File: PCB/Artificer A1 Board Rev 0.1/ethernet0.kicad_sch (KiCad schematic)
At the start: 32 parts, among them U14 RTL8211F-CG, X1 25MHz

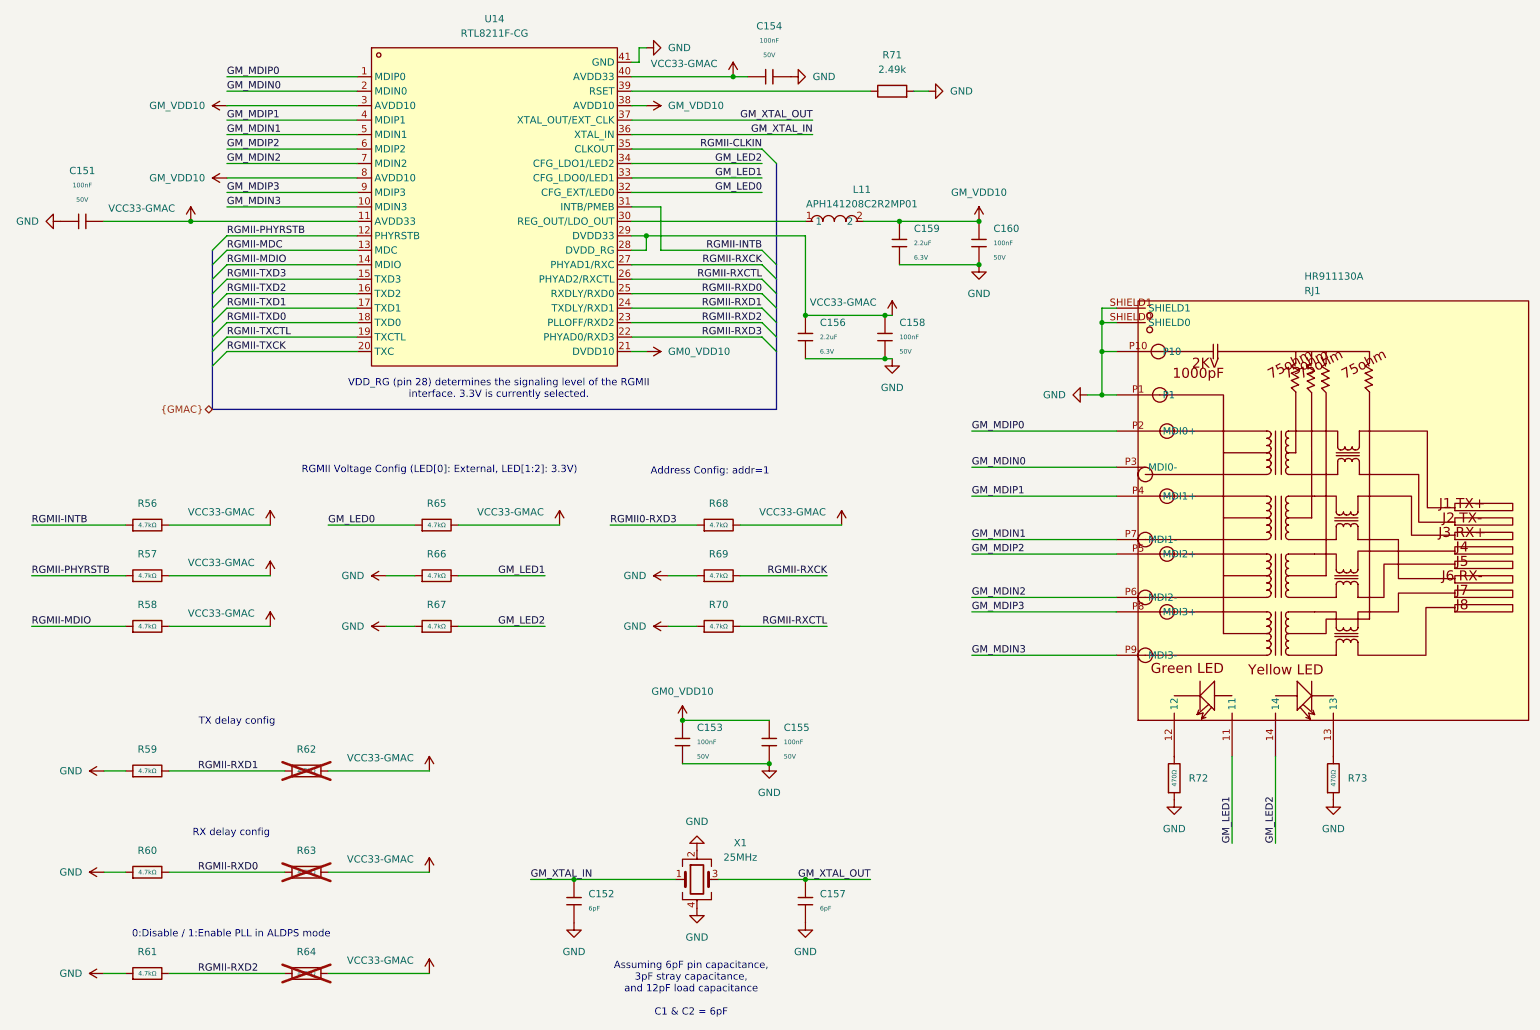
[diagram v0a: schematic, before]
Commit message: placed all components
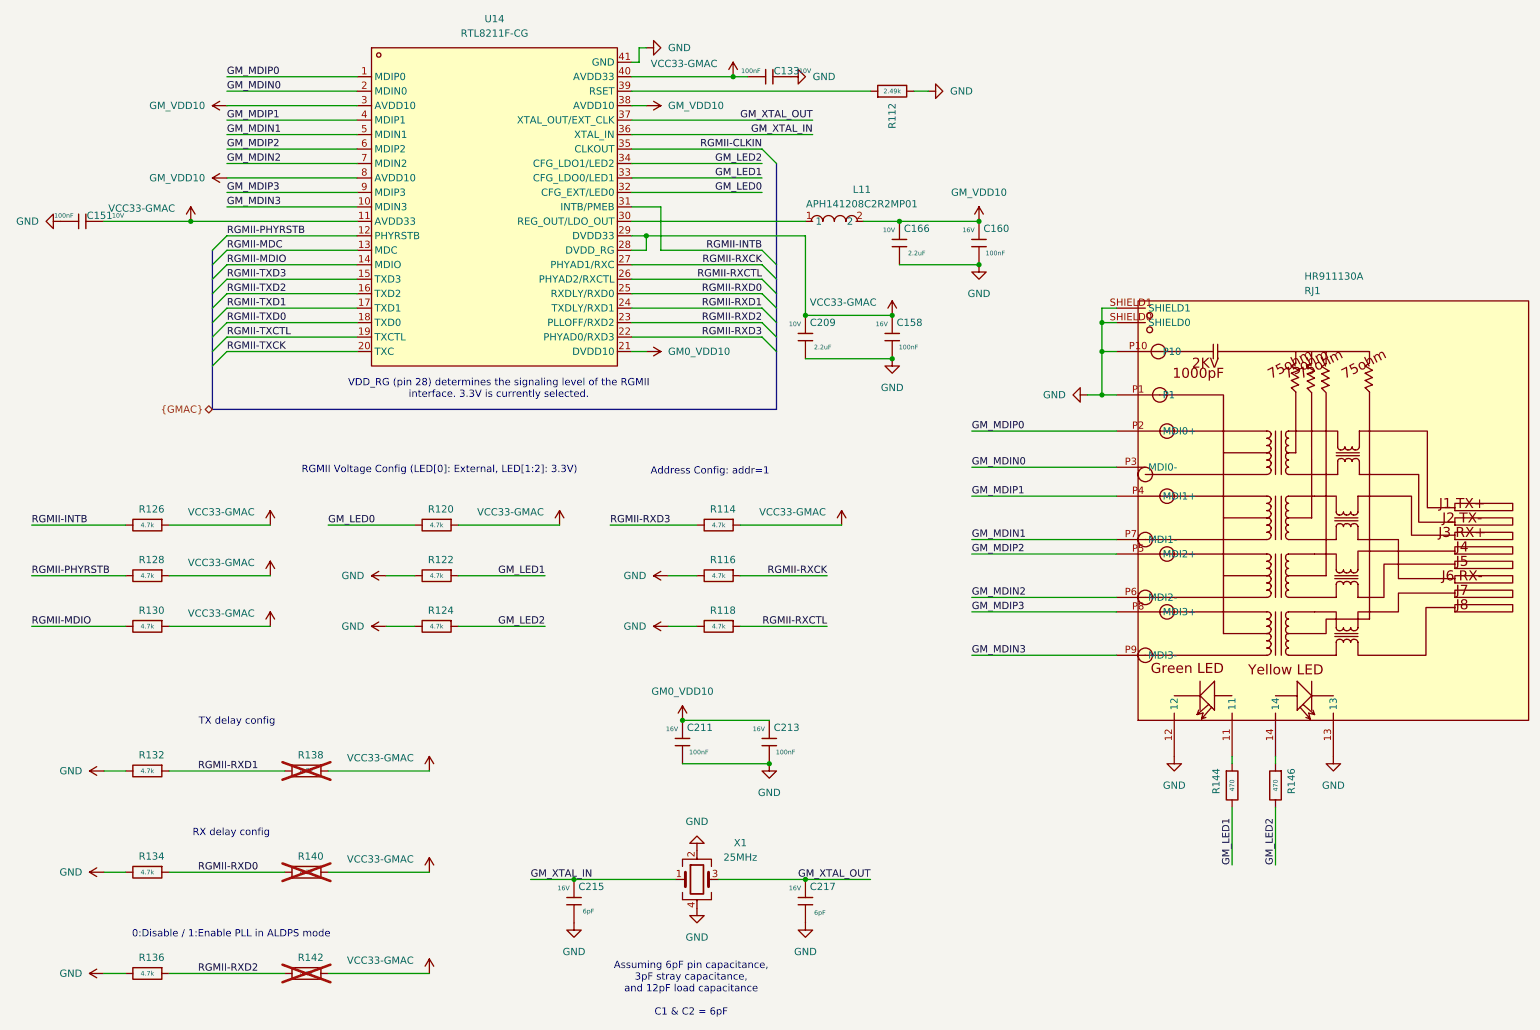
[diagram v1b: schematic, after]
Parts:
- removed C151, C153, C154, C155, C158, C160: 100nF, PCM_JLCPCB:C_0402, symbol PCM_JLCPCB-Capacitors:0402,100nF,(2)
- removed C152, C157: 6pF, PCM_JLCPCB:C_0402, symbol PCM_JLCPCB-Capacitors:0402,6pF
- removed C156, C159: 2.2uF, PCM_JLCPCB:C_0402, symbol PCM_JLCPCB-Capacitors:0402,2.2uF
- removed R56, R57, R58, R59, R60, R61, R62, R63, R64, R65, R66, R67, R68, R69, R70: 4.7kΩ, PCM_JLCPCB:R_0402, symbol PCM_JLCPCB-Resistors:0402,4.7kΩ
- removed R71: 2.49k, PCM_JLCPCB:R_0402, symbol Device:R
- removed R72, R73: 470Ω, PCM_JLCPCB:R_0402, symbol PCM_JLCPCB-Resistors:0402,470Ω
- added C133, C151, C158, C160, C211, C213: 100nF, Capacitor_SMD:C_0201_0603Metric, symbol Cap:JLCPCB_Lib_Blank_Cap
- added C166, C209: 2.2uF, Capacitor_SMD:C_0201_0603Metric, symbol Cap:JLCPCB_Lib_Blank_Cap
- added C215, C217: 6pF, Capacitor_SMD:C_0201_0603Metric, symbol Cap:JLCPCB_Lib_Blank_Cap
- added R112: 2.49k, Resistor_SMD:R_0201_0603Metric, symbol Cap:JLCPCB_Res_Custom
- added R114, R116, R118, R120, R122, R124, R126, R128, R130, R132, R134, R136, R138, R140, R142: 4.7k, Resistor_SMD:R_0201_0603Metric, symbol Cap:JLCPCB_Res_Custom
- added R144, R146: 470, Resistor_SMD:R_0201_0603Metric, symbol Cap:JLCPCB_Res_Custom
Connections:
- net GM0_VDD10: now also C211.2, C213.2
- net GM_LED0: now also R120.2
- net GM_LED1: now also R122.1, R144.2; no longer RJ1.11
- net GM_LED2: now also R124.1, R146.2; no longer RJ1.14
- net GM_VDD10: now also C160.2, C166.2
- net GM_XTAL_IN: now also C215.2
- net GM_XTAL_OUT: now also C217.2
- net GND: now also RJ1.12, RJ1.13, C133.2, C151.1, C158.1, C160.1, C166.1, C209.1, C211.1, C213.1, C215.1, C217.1, R112.2, R116.2, R118.2, R122.2, R124.2, R132.2, R134.2, R136.2
- net RGMII-INTB: now also R126.2
- net RGMII-MDIO: now also R130.2
- net RGMII-PHYRSTB: now also R128.2
- net RGMII-RXCK: now also R116.1
- net RGMII-RXCTL: now also R118.1
- net RGMII-RXD0: now also R134.1, R140.2
- net RGMII-RXD1: now also R132.1, R138.2
- net RGMII-RXD2: now also R136.1, R142.2
- net RGMII-RXD3: now also R114.2
- net VCC33-GMAC: now also C133.1, C151.2, C158.2, C209.2, R114.1, R120.1, R126.1, R128.1, R130.1, R138.1, R140.1, R142.1
- net at U14.39 (RSET): now also R112.1
- new net: R144.1, RJ1.11
- new net: R146.1, RJ1.14

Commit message: started routing
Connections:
- net GM_MDIN0 renamed GM_MDI0N
- net GM_MDIN1 renamed GM_MDI1N
- net GM_MDIN2 renamed GM_MDI2N
- net GM_MDIN3 renamed GM_MDI3N
- net GM_MDIP0 renamed GM_MDI0P
- net GM_MDIP1 renamed GM_MDI1P
- net GM_MDIP2 renamed GM_MDI2P
- net GM_MDIP3 renamed GM_MDI3P
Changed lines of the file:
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@@
 		)
 	)
-	(label "GM_MDIN0"
+	(label "GM_MDI0N"
 		(at 182.88 95.25 0)
 		(effects
@@
 		)
 	)
-	(label "GM_MDIP1"
+	(label "GM_MDI1P"
 		(at 52.07 34.29 0)
 		(effects
@@
 		)
 	)
-	(label "GM_MDIN3"
+	(label "GM_MDI3N"
 		(at 182.88 128.27 0)
 		(effects
@@
 		)
 	)
-	(label "GM_MDIN3"
+	(label "GM_MDI3N"
 		(at 52.07 49.53 0)
 		(effects
@@
 		)
 	)
-	(label "GM_MDIP0"
+	(label "GM_MDI0P"
 		(at 52.07 26.67 0)
 		(effects
@@
 		)
 	)
-	(label "GM_MDIN0"
+	(label "GM_MDI0N"
 		(at 52.07 29.21 0)
 		(effects
@@
 		)
 	)
-	(label "GM_MDIN1"
+	(label "GM_MDI1N"
 		(at 52.07 36.83 0)
 		(effects
@@
 		)
 	)
-	(label "GM_MDIP2"
+	(label "GM_MDI2P"
 		(at 182.88 110.49 0)
 		(effects
@@
 		)
 	)
-	(label "GM_MDIN1"
+	(label "GM_MDI1N"
 		(at 182.88 107.95 0)
 		(effects
@@
 		)
 	)
-	(label "GM_MDIP2"
+	(label "GM_MDI2P"
 		(at 52.07 39.37 0)
 		(effects
@@
 		)
 	)
-	(label "GM_MDIN2"
+	(label "GM_MDI2N"
 		(at 52.07 41.91 0)
 		(effects
@@
 		)
 	)
-	(label "GM_MDIP1"
+	(label "GM_MDI1P"
 		(at 182.88 100.33 0)
 		(effects
@@
 		)
 	)
-	(label "GM_MDIP3"
+	(label "GM_MDI3P"
 		(at 182.88 120.65 0)
 		(effects
@@
 		)
 	)
-	(label "GM_MDIP3"
+	(label "GM_MDI3P"
 		(at 52.07 46.99 0)
 		(effects
@@
 		)
 	)
-	(label "GM_MDIN2"
+	(label "GM_MDI2N"
 		(at 182.88 118.11 0)
 		(effects
@@
 		)
 	)
-	(label "GM_MDIP0"
+	(label "GM_MDI0P"
 		(at 182.88 88.9 0)
 		(effects
@@
 		(exclude_from_sim no)
 		(in_bom no)
-		(on_board yes)
-		(in_pos_files yes)
+		(on_board no)
+		(in_pos_files no)
 		(dnp yes)
 		(property "Reference" "R142"
@@
 		(exclude_from_sim no)
 		(in_bom no)
-		(on_board yes)
-		(in_pos_files yes)
+		(on_board no)
+		(in_pos_files no)
 		(dnp yes)
 		(property "Reference" "R138"
@@
 		(exclude_from_sim no)
 		(in_bom no)
-		(on_board yes)
-		(in_pos_files yes)
+		(on_board no)
+		(in_pos_files no)
 		(dnp yes)
 		(property "Reference" "R140"

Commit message: more power changed mipi csi and dis to aux 3.3V
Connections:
- net GM0_VDD10 is gone; now on net GM_VDD10: C211.2, C213.2, U14.21 (DVDD10)
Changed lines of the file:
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@@
 	)
 	(junction
+		(at 132.08 139.7)
+		(diameter 0)
+		(color 0 0 0 0)
+	)
+	(junction
 		(at 153.67 68.58)
 		(diameter 0)
@@
 		(color 0 0 0 0)
 	)
-	(junction
-		(at 132.08 139.7)
-		(diameter 0)
-		(color 0 0 0 0)
-	)
 	(bus_entry
 		(at 49.53 59.69)
@@
 	)
 	(symbol
-		(lib_id "power:+1V0")
-		(at 132.08 139.7 0)
-		(unit 1)
-		(body_style 1)
-		(exclude_from_sim no)
-		(in_bom yes)
-		(on_board yes)
-		(in_pos_files yes)
-		(dnp no)
-		(fields_autoplaced yes)
-		(property "Reference" "#PWR0305"
-			(at 132.08 143.51 0)
-			(hide yes)
-			(show_name no)
-			(do_not_autoplace no)
-			(effects
-				(font
-					(size 1.27 1.27)
-				)
-			)
-		)
-		(property "Value" "GM0_VDD10"
-			(at 132.08 134.62 0)
-			(show_name no)
-			(do_not_autoplace no)
-			(effects
-				(font
-					(size 1.27 1.27)
-				)
-			)
-		)
-		(property "Footprint" ""
-			(at 132.08 139.7 0)
-			(hide yes)
-			(show_name no)
-			(do_not_autoplace no)
-			(effects
-				(font
-					(size 1.27 1.27)
-				)
-			)
-		)
-		(property "Datasheet" ""
-			(at 132.08 139.7 0)
-			(hide yes)
-			(show_name no)
-			(do_not_autoplace no)
-			(effects
-				(font
-					(size 1.27 1.27)
-				)
-			)
-		)
-		(property "Description" "Power symbol creates a global label with name \"+1V0\""
-			(at 132.08 139.7 0)
-			(hide yes)
-			(show_name no)
-			(do_not_autoplace no)
-			(effects
-				(font
-					(size 1.27 1.27)
-				)
-			)
-		)
-		(pin "1"
-		)
-		(instances
-			(project "Artificer A1 Board Rev 0.1"
-				(path "/7c37bdb5-94b0-4567-b5ec-a879db855389/8dbcd277-0044-4a46-a7d8-a4fbff98b8e0"
-					(reference "#PWR0305")
-					(unit 1)
-				)
-				(path "/7c37bdb5-94b0-4567-b5ec-a879db855389/acce53b9-49b8-45d6-9f6f-dde333340d83"
-					(reference "#PWR0343")
-					(unit 1)
-				)
-			)
-		)
-	)
-	(symbol
 		(lib_id "Cap:JLCPCB_Res_Custom")
 		(at 38.1 148.59 270)
@@
 	)
 	(symbol
+		(lib_name "+1V0_1")
+		(lib_id "power:+1V0")
+		(at 125.73 74.93 270)
+		(unit 1)
+		(body_style 1)
+		(exclude_from_sim no)
+		(in_bom yes)
+		(on_board yes)
+		(in_pos_files yes)
+		(dnp no)
+		(fields_autoplaced yes)
+		(property "Reference" "#PWR0340"
+			(at 121.92 74.93 0)
+			(hide yes)
+			(show_name no)
+			(do_not_autoplace no)
+			(effects
+				(font
+					(size 1.27 1.27)
+				)
+			)
+		)
+		(property "Value" "GM_VDD10"
+			(at 129.54 74.9299 90)
+			(show_name no)
+			(do_not_autoplace no)
+			(effects
+				(font
+					(size 1.27 1.27)
+				)
+				(justify left)
+			)
+		)
+		(property "Footprint" ""
+			(at 125.73 74.93 0)
+			(hide yes)
+			(show_name no)
+			(do_not_autoplace no)
+			(effects
+				(font
+					(size 1.27 1.27)
+				)
+			)
+		)
+		(property "Datasheet" ""
+			(at 125.73 74.93 0)
+			(hide yes)
+			(show_name no)
+			(do_not_autoplace no)
+			(effects
+				(font
+					(size 1.27 1.27)
+				)
+			)
+		)
+		(property "Description" ""
+			(at 125.73 74.93 0)
+			(hide yes)
+			(show_name no)
+			(do_not_autoplace no)
+			(effects
+				(font
+					(size 1.27 1.27)
+				)
+			)
+		)
+		(pin "1"
+		)
+		(instances
+			(project "Artificer A1 Board Rev 0.1"
+				(path "/7c37bdb5-94b0-4567-b5ec-a879db855389/8dbcd277-0044-4a46-a7d8-a4fbff98b8e0"
+					(reference "#PWR0340")
+					(unit 1)
+				)
+				(path "/7c37bdb5-94b0-4567-b5ec-a879db855389/acce53b9-49b8-45d6-9f6f-dde333340d83"
+					(reference "#PWR0591")
+					(unit 1)
+				)
+			)
+		)
+	)
+	(symbol
 		(lib_id "easyeda:APH141208C2R2MP01")
 		(at 158.75 52.07 0)
@@
 	)
 	(symbol
+		(lib_name "+1V0_1")
+		(lib_id "power:+1V0")
+		(at 132.08 139.7 0)
+		(unit 1)
+		(body_style 1)
+		(exclude_from_sim no)
+		(in_bom yes)
+		(on_board yes)
+		(in_pos_files yes)
+		(dnp no)
+		(fields_autoplaced yes)
+		(property "Reference" "#PWR0343"
+			(at 132.08 143.51 0)
+			(hide yes)
+			(show_name no)
+			(do_not_autoplace no)
+			(effects
+				(font
+					(size 1.27 1.27)
+				)
+			)
+		)
+		(property "Value" "GM_VDD10"
+			(at 132.08 134.62 0)
+			(show_name no)
+			(do_not_autoplace no)
+			(effects
+				(font
+					(size 1.27 1.27)
+				)
+			)
+		)
+		(property "Footprint" ""
+			(at 132.08 139.7 0)
+			(hide yes)
+			(show_name no)
+			(do_not_autoplace no)
+			(effects
+				(font
+					(size 1.27 1.27)
+				)
+			)
+		)
+		(property "Datasheet" ""
+			(at 132.08 139.7 0)
+			(hide yes)
+			(show_name no)
+			(do_not_autoplace no)
+			(effects
+				(font
+					(size 1.27 1.27)
+				)
+			)
+		)
+		(property "Description" ""
+			(at 132.08 139.7 0)
+			(hide yes)
+			(show_name no)
+			(do_not_autoplace no)
+			(effects
+				(font
+					(size 1.27 1.27)
+				)
+			)
+		)
+		(pin "1"
+		)
+		(instances
+			(project "Artificer A1 Board Rev 0.1"
+				(path "/7c37bdb5-94b0-4567-b5ec-a879db855389/8dbcd277-0044-4a46-a7d8-a4fbff98b8e0"
+					(reference "#PWR0343")
+					(unit 1)
+				)
+				(path "/7c37bdb5-94b0-4567-b5ec-a879db855389/acce53b9-49b8-45d6-9f6f-dde333340d83"
+					(reference "#PWR0590")
+					(unit 1)
+				)
+			)
+		)
+	)
+	(symbol
 		(lib_id "easyeda:HR911130A")
 		(at 241.3 106.68 0)
@@
 					(unit 1)
 				)
-			)
-		)
-	)
-	(symbol
-		(lib_id "power:+1V0")
-		(at 125.73 74.93 270)
-		(unit 1)
-		(body_style 1)
-		(exclude_from_sim no)
-		(in_bom yes)
-		(on_board yes)
-		(in_pos_files yes)
-		(dnp no)
-		(fields_autoplaced yes)
-		(property "Reference" "#PWR0302"
-			(at 121.92 74.93 0)
-			(hide yes)
-			(show_name no)
-			(do_not_autoplace no)
-			(effects
-				(font
-					(size 1.27 1.27)
-				)
-			)
-		)
-		(property "Value" "GM0_VDD10"
-			(at 129.54 74.9299 90)
-			(show_name no)
-			(do_not_autoplace no)
-			(effects
-				(font
-					(size 1.27 1.27)
-				)
-				(justify left)
-			)
-		)
-		(property "Footprint" ""
-			(at 125.73 74.93 0)
-			(hide yes)
-			(show_name no)
-			(do_not_autoplace no)
-			(effects
-				(font
-					(size 1.27 1.27)
-				)
-			)
-		)
-		(property "Datasheet" ""
-			(at 125.73 74.93 0)
-			(hide yes)
-			(show_name no)
-			(do_not_autoplace no)
-			(effects
-				(font
-					(size 1.27 1.27)
-				)
-			)
-		)
-		(property "Description" "Power symbol creates a global label with name \"+1V0\""
-			(at 125.73 74.93 0)
-			(hide yes)
-			(show_name no)
-			(do_not_autoplace no)
-			(effects
-				(font
-					(size 1.27 1.27)
-				)
-			)
-		)
-		(pin "1"
-		)
-		(instances
-			(project "Artificer A1 Board Rev 0.1"
-				(path "/7c37bdb5-94b0-4567-b5ec-a879db855389/8dbcd277-0044-4a46-a7d8-a4fbff98b8e0"
-					(reference "#PWR0302")
-					(unit 1)
-				)
-				(path "/7c37bdb5-94b0-4567-b5ec-a879db855389/acce53b9-49b8-45d6-9f6f-dde333340d83"
-					(reference "#PWR0340")
-					(unit 1)
-				)
